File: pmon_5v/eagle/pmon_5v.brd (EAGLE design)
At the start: 60 x 60 mm, 30 parts, among them J1 USB, J2 USB, J3 USB_A, J4 PINHD-2X3, Q1 16Mhz, U1 LTC2943, U2 FT232RL, U3 ATMEGA328TQFP32

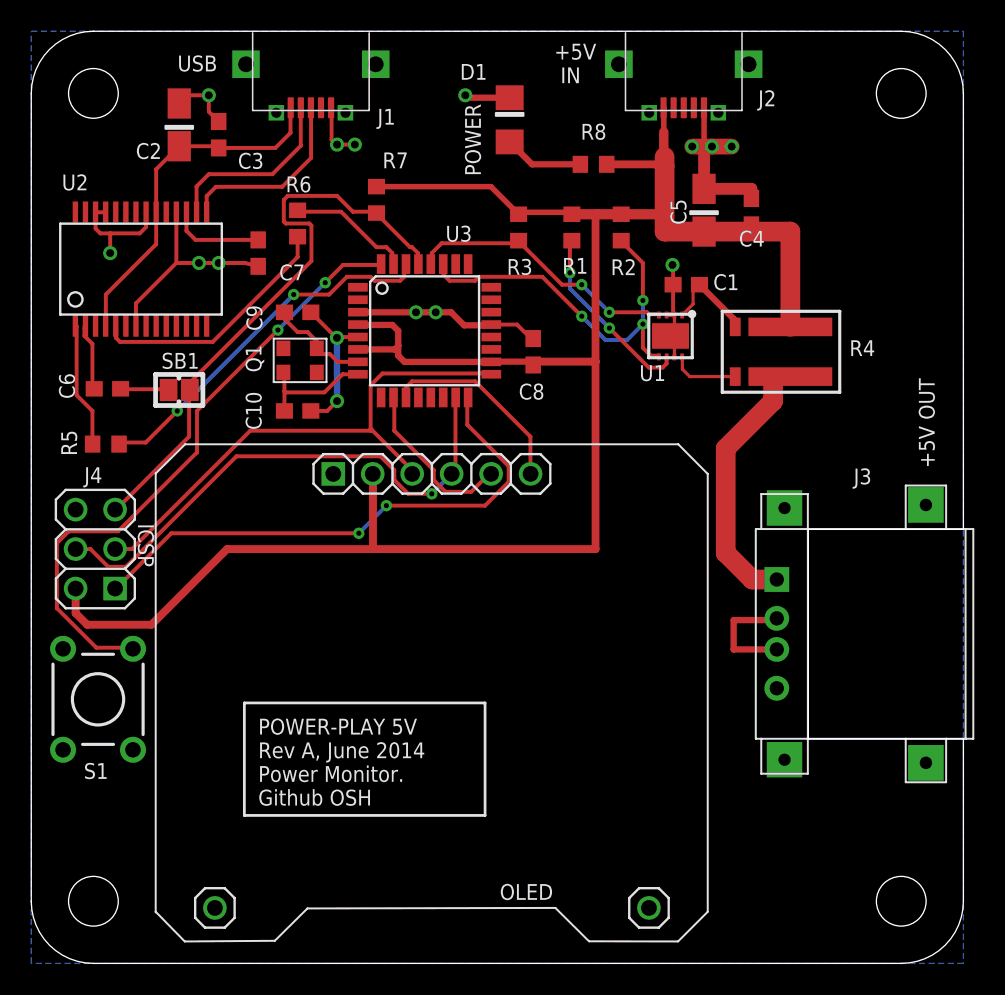
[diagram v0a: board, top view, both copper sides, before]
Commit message: Removed power led, added vias to the solder jumpers.
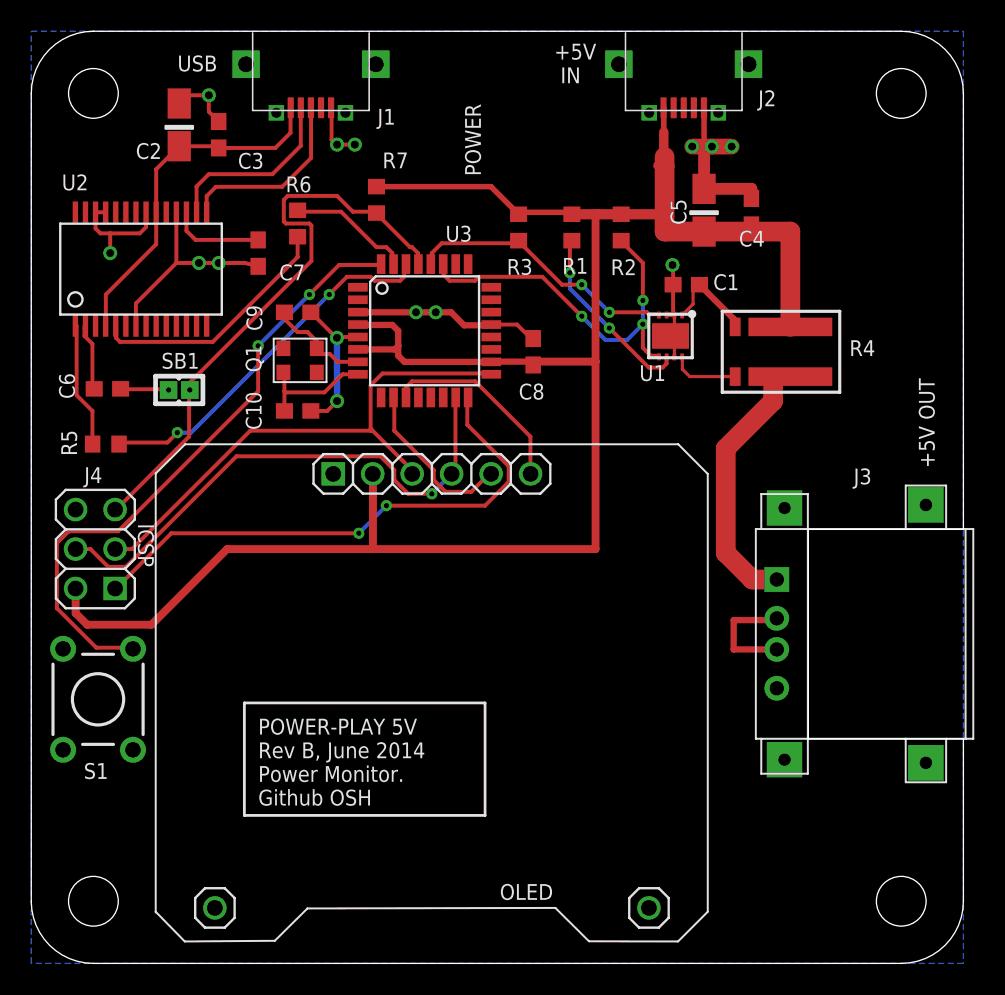
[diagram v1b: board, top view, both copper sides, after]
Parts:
- removed D1: BLUE, pmon_5v:1206-LED
- removed R8: 3K3, pmon_5v:R0603
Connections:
- removed net N$17: D1.A, R8.2
- net +5V: no longer R8.1
- net GND: no longer D1.C
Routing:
- net N$17: track 5.15 -> 0.00 mm
- net +5V: track 133.1 -> 129.9 mm
- net GND: track 74.8 -> 71.9 mm, vias 15 -> 14
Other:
- board text added: "POWER-PLAY 5V - REV B OSH GITHUB"
- board text added: "POWER-PLAY 5V Rev B, June 2014 Power Monitor. Github OSH"
- board text removed: "POWER-PLAY 5V - REV A OSH GITHUB"
- board text removed: "POWER-PLAY 5V Rev A, June 2014 Power Monitor. Github OSH"
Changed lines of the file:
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@@
 <layer number="27" name="tValues" color="7" fill="1" visible="yes" active="yes"/>
 <layer number="28" name="bValues" color="7" fill="1" visible="yes" active="yes"/>
-<layer number="29" name="tStop" color="7" fill="3" visible="yes" active="yes"/>
-<layer number="30" name="bStop" color="7" fill="6" visible="yes" active="yes"/>
+<layer number="29" name="tStop" color="7" fill="3" visible="no" active="yes"/>
+<layer number="30" name="bStop" color="7" fill="6" visible="no" active="yes"/>
 <layer number="31" name="tCream" color="7" fill="4" visible="yes" active="yes"/>
 <layer number="32" name="bCream" color="7" fill="5" visible="yes" active="yes"/>
@@
 <circle x="56" y="4" radius="3" width="0.4064" layer="42"/>
 <text x="14.605" y="10.16" size="1.016" layer="21" font="vector" ratio="10" rot="SR0">POWER-PLAY 5V
-Rev A, June 2014
+Rev B, June 2014
 Power Monitor.
 Github OSH</text>
@@
 <text x="28.94211875" y="50.680546875" size="1.016" layer="21" ratio="10" rot="R90">POWER</text>
 <text x="6.87123125" y="28.31666875" size="1.016" layer="21" ratio="10" rot="SR270">ICSP</text>
-<text x="16.002" y="2.286" size="1.016" layer="30" font="vector" ratio="15" rot="SMR0" align="bottom-right">POWER-PLAY 5V - REV A
+<text x="16.002" y="2.286" size="1.016" layer="30" font="vector" ratio="15" rot="SMR0" align="bottom-right">POWER-PLAY 5V - REV B
 OSH GITHUB</text>
 <text x="58.15211875" y="31.884546875" size="1.016" layer="21" ratio="10" rot="R90">+5V OUT</text>
@@
 <attribute name="NAME" x="6.72763125" y="51.781690625" size="1.016" layer="25" font="vector" ratio="10"/>
 </element>
-<element name="D1" library="pmon_5v" package="1206-LED" value="BLUE" x="30.795" y="54.3" smashed="yes" rot="R90">
-<attribute name="NAME" x="29.354934375" y="57.894621875" size="1.016" layer="25" font="vector" ratio="10" rot="R180"/>
-</element>
-<element name="R8" library="pmon_5v" package="R0603" value="3K3" x="36.195" y="51.435" smashed="yes" rot="R180">
-<attribute name="NAME" x="35.364328125" y="53.024765625" size="1.016" layer="25" font="vector" ratio="10"/>
-</element>
 <element name="C7" library="pmon_5v" package="C0603" value="0.1uF" x="14.605" y="45.72" smashed="yes" rot="R270">
 <attribute name="NAME" x="15.956221875" y="43.969615625" size="1.016" layer="25" font="vector" ratio="10"/>
@@
 <contactref element="U3" pad="3"/>
 <contactref element="U3" pad="21"/>
-<contactref element="D1" pad="C"/>
 <contactref element="C3" pad="2"/>
 <contactref element="J2" pad="5"/>
@@
 <wire x1="19.685" y1="31.75" x2="19.558" y2="31.623" width="0.508" layer="16"/>
 <wire x1="19.558" y1="31.623" x2="19.4818" y2="31.5468" width="0.508" layer="16"/>
-<wire x1="30.795" y1="55.722" x2="28.098" y2="55.722" width="0.4064" layer="1"/>
-<wire x1="28.098" y1="55.722" x2="27.94" y2="55.88" width="0.4064" layer="1"/>
-<via x="27.94" y="55.88" extent="1-16" drill="0.508"/>
 <contactref element="S1" pad="A"/>
 <wire x1="43.815" y1="52.578" x2="45.085" y2="52.578" width="1.016" layer="1"/>
@@
 <contactref element="U3" pad="4"/>
 <contactref element="U3" pad="6"/>
-<contactref element="R8" pad="1"/>
 <contactref element="R2" pad="2"/>
 <contactref element="R3" pad="2"/>
@@
 <wire x1="32.385" y1="38.735" x2="32.3088" y2="38.6588" width="0.254" layer="1"/>
 <wire x1="32.3088" y1="38.6588" x2="32.3088" y2="38.52" width="0.254" layer="1"/>
-<wire x1="40.2336" y1="51.435" x2="37.045" y2="51.435" width="0.508" layer="1"/>
-<wire x1="37.045" y1="51.435" x2="37.084" y2="51.396" width="0.508" layer="1"/>
 <wire x1="21.98" y1="31.51" x2="21.9964" y2="31.4936" width="0.508" layer="1"/>
 <wire x1="21.9964" y1="31.4936" x2="21.9964" y2="26.67" width="0.508" layer="1"/>
@@
 <wire x1="10.287" y1="36.957" x2="10.2108" y2="36.91" width="0.254" layer="1"/>
 </signal>
-<signal name="N$17">
-<contactref element="D1" pad="A"/>
-<contactref element="R8" pad="2"/>
-<wire x1="35.345" y1="51.435" x2="32.238" y2="51.435" width="0.4064" layer="1"/>
-<wire x1="32.238" y1="51.435" x2="30.795" y2="52.878" width="0.4064" layer="1"/>
-</signal>
 <signal name="SCK">
 <contactref element="J4" pad="3"/>
@@
 <contactref element="U3" pad="30"/>
 <contactref element="R5" pad="1"/>
-<wire x1="7.366" y1="33.528" x2="5.715" y2="33.528" width="0.254" layer="1"/>
-<wire x1="9.398" y1="35.56" x2="7.366" y2="33.528" width="0.254" layer="1"/>
-<wire x1="16.891" y1="43.053" x2="9.398" y2="35.56" width="0.254" layer="16"/>
-<wire x1="19.177" y1="43.053" x2="16.891" y2="43.053" width="0.254" layer="1"/>
+<wire x1="8.763" y1="33.528" x2="5.715" y2="33.528" width="0.254" layer="1"/>
+<wire x1="9.398" y1="34.163" x2="8.763" y2="33.528" width="0.254" layer="1"/>
+<wire x1="10.287" y1="34.163" x2="9.398" y2="34.163" width="0.254" layer="16"/>
+<wire x1="19.177" y1="43.053" x2="10.287" y2="34.163" width="0.254" layer="16"/>
 <wire x1="20.32" y1="44.196" x2="19.177" y2="43.053" width="0.254" layer="1"/>
 <wire x1="21.844" y1="44.196" x2="20.32" y2="44.196" width="0.254" layer="1"/>
@@
 <wire x1="5.715" y1="33.528" x2="5.6506" y2="33.4264" width="0.254" layer="1"/>
 <wire x1="24.003" y1="44.958" x2="24.12" y2="45.0126" width="0.254" layer="1"/>
-<via x="9.398" y="35.56" extent="1-16" drill="0.3302"/>
-<via x="16.891" y="43.053" extent="1-16" drill="0.3302"/>
+<via x="9.398" y="34.163" extent="1-16" drill="0.3302"/>
+<via x="19.177" y="43.053" extent="1-16" drill="0.3302"/>
 </signal>
 <signal name="SER_TX">
@@
 <contactref element="U3" pad="32"/>
 <contactref element="S1" pad="B"/>
-<wire x1="20.066" y1="44.958" x2="22.479" y2="44.958" width="0.254" layer="1"/>
-<wire x1="18.923" y1="43.815" x2="20.066" y2="44.958" width="0.254" layer="1"/>
-<wire x1="15.875" y1="40.767" x2="18.923" y2="43.815" width="0.254" layer="16"/>
-<wire x1="10.668" y1="35.56" x2="15.875" y2="40.767" width="0.254" layer="1"/>
-<wire x1="10.668" y1="32.893" x2="10.668" y2="35.56" width="0.254" layer="1"/>
-<wire x1="5.588" y1="27.813" x2="10.668" y2="32.893" width="0.254" layer="1"/>
+<wire x1="19.812" y1="44.958" x2="22.479" y2="44.958" width="0.254" layer="1"/>
+<wire x1="17.907" y1="43.053" x2="19.812" y2="44.958" width="0.254" layer="1"/>
+<wire x1="14.605" y1="39.751" x2="17.907" y2="43.053" width="0.254" layer="16"/>
+<wire x1="14.605" y1="36.83" x2="14.605" y2="39.751" width="0.254" layer="1"/>
+<wire x1="5.588" y1="27.813" x2="14.605" y2="36.83" width="0.254" layer="1"/>
 <wire x1="2.413" y1="27.813" x2="5.588" y2="27.813" width="0.254" layer="1"/>
 <wire x1="1.651" y1="27.051" x2="2.413" y2="27.813" width="0.254" layer="1"/>
@@
 <wire x1="22.479" y1="44.958" x2="22.52" y2="45.0126" width="0.254" layer="1"/>
 <wire x1="6.477" y1="20.32" x2="6.54768125" y2="20.24768125" width="0.254" layer="1"/>
-<via x="18.923" y="43.815" extent="1-16" drill="0.3302"/>
-<via x="15.875" y="40.767" extent="1-16" drill="0.3302"/>
+<via x="17.907" y="43.053" extent="1-16" drill="0.3302"/>
+<via x="14.605" y="39.751" extent="1-16" drill="0.3302"/>
 </signal>
 <signal name="DEBUG">

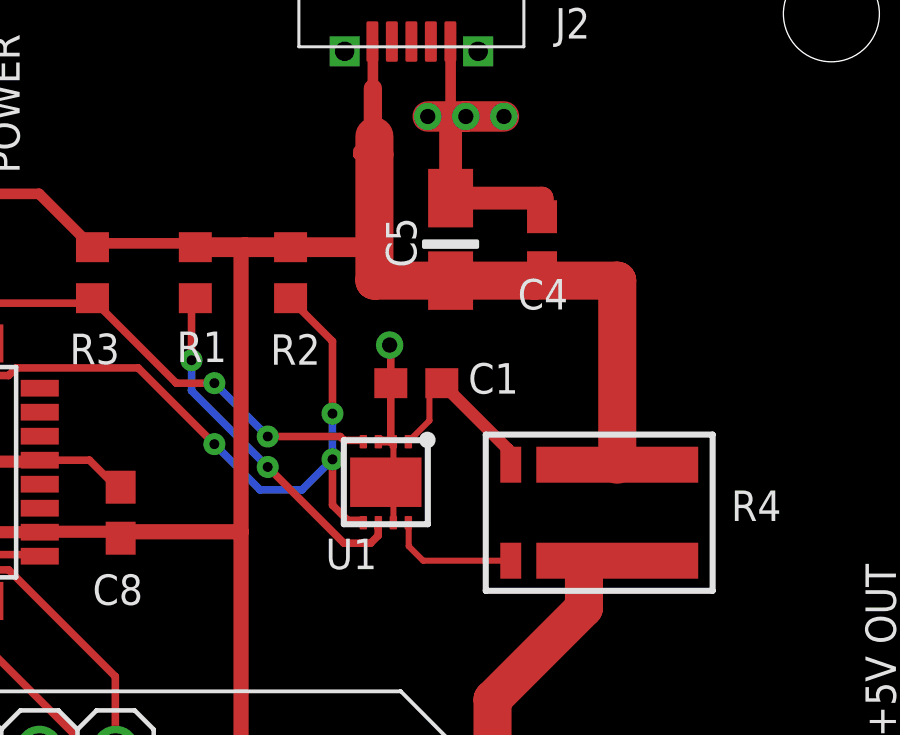
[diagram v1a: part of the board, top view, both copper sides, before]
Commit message: Updated the LTC2943 footpting to match the datasheet (longer pads now).
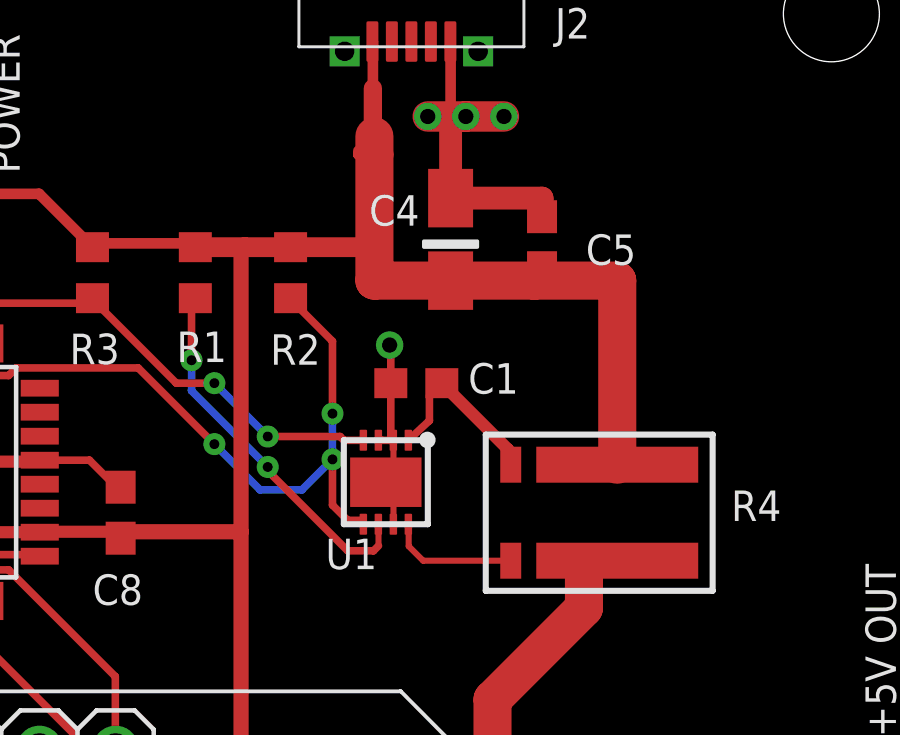
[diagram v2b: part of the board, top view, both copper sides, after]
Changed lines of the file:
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@@
 <layer number="28" name="bValues" color="7" fill="1" visible="yes" active="yes"/>
 <layer number="29" name="tStop" color="7" fill="3" visible="no" active="yes"/>
-<layer number="30" name="bStop" color="7" fill="6" visible="no" active="yes"/>
+<layer number="30" name="bStop" color="7" fill="6" visible="yes" active="yes"/>
 <layer number="31" name="tCream" color="7" fill="4" visible="yes" active="yes"/>
 <layer number="32" name="bCream" color="7" fill="5" visible="yes" active="yes"/>
@@
 </element>
 <element name="C4" library="pmon_5v" package="A/3216-18R" value="10uF" x="43.307" y="48.481" smashed="yes" rot="R270">
-<attribute name="NAME" x="45.546409375" y="46.14461875" size="1.016" layer="25" font="vector" ratio="10"/>
+<attribute name="NAME" x="40.593409375" y="48.93861875" size="1.016" layer="25" font="vector" ratio="10"/>
 </element>
 <element name="C5" library="pmon_5v" package="C0603" value="0.1uF" x="46.355" y="48.387" smashed="yes" rot="R90">
-<attribute name="NAME" x="42.168634375" y="47.538015625" size="1.016" layer="25" font="vector" ratio="10" rot="R90"/>
+<attribute name="NAME" x="49.489984375" y="48.645634375" size="1.016" layer="25" font="vector" ratio="10" rot="R180"/>
 </element>
 <element name="C1" library="pmon_5v" package="C0603" value="1uF" x="42.164" y="43.688" smashed="yes" rot="R180">
@@
 <via x="26.035" y="41.91" extent="1-16" drill="0.508"/>
 <via x="24.765" y="41.91" extent="1-16" drill="0.508"/>
-<wire x1="41.398" y1="41.736" x2="41.402" y2="41.74" width="0.2032" layer="1"/>
-<wire x1="41.398" y1="41.736" x2="41.402" y2="41.732" width="0.2032" layer="1"/>
+<wire x1="41.398" y1="41.786" x2="41.402" y2="41.74" width="0.2032" layer="1"/>
+<wire x1="41.398" y1="41.786" x2="41.402" y2="41.732" width="0.2032" layer="1"/>
 <wire x1="41.402" y1="41.732" x2="41.402" y2="40.9956" width="0.2032" layer="1"/>
 <wire x1="41.402" y1="40.9956" x2="41.148" y2="40.7416" width="0.2032" layer="1"/>
 <wire x1="41.148" y1="40.7416" x2="41.148" y2="40.386" width="0.2032" layer="1"/>
-<wire x1="41.398" y1="39.036" x2="41.402" y2="39.04" width="0.2032" layer="1"/>
+<wire x1="41.398" y1="38.986" x2="41.402" y2="39.04" width="0.2032" layer="1"/>
 <wire x1="41.402" y1="39.04" x2="41.402" y2="39.7764" width="0.2032" layer="1"/>
 <wire x1="41.402" y1="39.7764" x2="41.148" y2="40.0304" width="0.2032" layer="1"/>
@@
 <via x="20.828" y="52.705" extent="1-16" drill="0.508"/>
 <wire x1="19.685" y1="52.705" x2="20.828" y2="52.705" width="0.254" layer="1"/>
-<wire x1="41.021" y1="41.783" x2="40.898" y2="41.736" width="0.254" layer="1"/>
-<wire x1="41.275" y1="41.783" x2="41.398" y2="41.736" width="0.254" layer="1"/>
+<wire x1="41.021" y1="41.783" x2="40.898" y2="41.786" width="0.254" layer="1"/>
+<wire x1="41.275" y1="41.783" x2="41.398" y2="41.786" width="0.254" layer="1"/>
 <contactref element="J3" pad="4"/>
 <wire x1="43.3" y1="55.075" x2="43.307" y2="55.075" width="0.3556" layer="1"/>
@@
 <wire x1="46.355" y1="49.856" x2="46.355" y2="49.237" width="0.762" layer="1"/>
 <wire x1="19.558" y1="31.623" x2="19.44" y2="31.51" width="0.254" layer="16"/>
-<wire x1="41.402" y1="38.989" x2="41.398" y2="39.036" width="0.254" layer="1"/>
+<wire x1="41.402" y1="38.989" x2="41.398" y2="38.986" width="0.254" layer="1"/>
 <wire x1="41.021" y1="41.783" x2="41.275" y2="41.783" width="0.254" layer="1"/>
 <wire x1="41.275" y1="41.783" x2="41.314" y2="41.783" width="0.254" layer="1"/>
 <wire x1="41.314" y1="41.783" x2="41.314" y2="43.688" width="0.254" layer="1"/>
-<wire x1="41.275" y1="41.783" x2="41.275" y2="41.736" width="0.254" layer="1"/>
-<wire x1="41.275" y1="41.736" x2="40.898" y2="41.736" width="0.254" layer="1"/>
 </signal>
 <signal name="+5V">
@@
 <contactref element="U1" pad="1"/>
 <wire x1="45.224" y1="40.97" x2="45.312" y2="40.97" width="0.2032" layer="1"/>
-<wire x1="41.898" y1="41.736" x2="42.6014375" y2="42.4394375" width="0.2032" layer="1"/>
-<wire x1="42.6014375" y1="42.4394375" x2="42.6014375" y2="43.2754375" width="0.2032" layer="1"/>
+<wire x1="41.898" y1="41.786" x2="42.6014375" y2="42.4394375" width="0.254" layer="1"/>
+<wire x1="42.6014375" y1="42.4394375" x2="42.6014375" y2="43.2754375" width="0.254" layer="1"/>
 <wire x1="42.6014375" y1="43.2754375" x2="43.014" y2="43.688" width="0.2032" layer="1"/>
 <wire x1="45.224" y1="40.97" x2="45.224" y2="41.478" width="0.4064" layer="1"/>
@@
 <contactref element="R4" pad="V1"/>
 <contactref element="U1" pad="8"/>
-<wire x1="41.898" y1="39.036" x2="41.91" y2="39.024" width="0.2032" layer="1"/>
+<wire x1="41.898" y1="38.986" x2="41.91" y2="39.024" width="0.2032" layer="1"/>
 <wire x1="41.91" y1="39.024" x2="41.91" y2="38.2524" width="0.2032" layer="1"/>
 <wire x1="41.91" y1="38.2524" x2="42.3924" y2="37.77" width="0.2032" layer="1"/>
@@
 <contactref element="U1" pad="4"/>
 <contactref element="U3" pad="28"/>
-<wire x1="40.386" y1="41.783" x2="40.398" y2="41.736" width="0.254" layer="1"/>
+<wire x1="40.386" y1="41.783" x2="40.398" y2="41.786" width="0.254" layer="1"/>
 <wire x1="25.781" y1="44.958" x2="25.72" y2="45.0126" width="0.254" layer="1"/>
 <wire x1="39.751" y1="41.783" x2="40.386" y2="41.783" width="0.254" layer="1"/>
@@
 <wire x1="39.37" y1="45.085" x2="39.37" y2="42.672" width="0.254" layer="1"/>
 <wire x1="37.973" y1="46.482" x2="39.37" y2="45.085" width="0.254" layer="1"/>
-<wire x1="40.386" y1="39.116" x2="40.398" y2="39.036" width="0.254" layer="1"/>
+<wire x1="40.386" y1="39.116" x2="40.398" y2="38.986" width="0.254" layer="1"/>
 <wire x1="37.973" y1="46.482" x2="37.973" y2="46.521" width="0.254" layer="1"/>
 <wire x1="26.543" y1="44.323" x2="26.543" y2="44.958" width="0.254" layer="1"/>
@@
 <contactref element="U1" pad="6"/>
 <contactref element="R1" pad="1"/>
-<wire x1="40.894" y1="38.989" x2="40.898" y2="39.036" width="0.254" layer="1"/>
-<wire x1="40.894" y1="38.608" x2="40.894" y2="38.862" width="0.254" layer="1"/>
-<wire x1="40.64" y1="38.354" x2="40.894" y2="38.608" width="0.254" layer="1"/>
-<wire x1="39.751" y1="38.354" x2="40.64" y2="38.354" width="0.254" layer="1"/>
-<wire x1="37.211" y1="40.894" x2="39.751" y2="38.354" width="0.254" layer="1"/>
+<wire x1="40.894" y1="38.989" x2="40.898" y2="38.986" width="0.254" layer="1"/>
 <wire x1="34.671" y1="43.434" x2="37.211" y2="40.894" width="0.254" layer="16"/>
 <wire x1="34.671" y1="44.45" x2="34.671" y2="43.434" width="0.254" layer="16"/>
 <wire x1="34.671" y1="46.355" x2="34.671" y2="44.45" width="0.254" layer="1"/>
 <wire x1="34.798" y1="46.482" x2="34.671" y2="46.355" width="0.254" layer="1"/>
-<wire x1="40.894" y1="38.862" x2="40.898" y2="39.036" width="0.254" layer="1"/>
 <wire x1="34.798" y1="46.482" x2="34.798" y2="46.521" width="0.254" layer="1"/>
 <via x="37.211" y="40.894" extent="1-16" drill="0.3302"/>
 <via x="34.671" y="44.45" extent="1-16" drill="0.3302"/>
+<wire x1="40.894" y1="38.862" x2="40.903490625" y2="38.862" width="0.2032" layer="1"/>
+<wire x1="40.903490625" y1="38.862" x2="40.903490625" y2="38.266165625" width="0.2032" layer="1"/>
+<wire x1="40.903490625" y1="38.266165625" x2="40.737325" y2="38.1" width="0.254" layer="1"/>
+<wire x1="40.737325" y1="38.1" x2="39.878" y2="38.1" width="0.254" layer="1"/>
+<wire x1="39.878" y1="38.1" x2="37.211" y2="40.767" width="0.254" layer="1"/>
+<wire x1="37.211" y1="40.767" x2="37.211" y2="40.894" width="0.254" layer="1"/>
+<wire x1="40.898" y1="38.986" x2="40.903490625" y2="38.980509375" width="0.2032" layer="1"/>
+<wire x1="40.903490625" y1="38.980509375" x2="40.903490625" y2="38.862" width="0.2032" layer="1"/>
 </signal>
 <signal name="N$22">
